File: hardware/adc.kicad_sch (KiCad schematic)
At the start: 21 parts, among them U5 NAU7802SGI, U7 NAU7802SGI

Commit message: Connect each ADC to a separate I2C bus
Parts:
- added R11, R12: 10kΩ, symbol Device:R_Small
- renumbered R11 to R13, R12 to R14
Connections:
- net +3.3V: now also R11.1, R12.1
- net SCLK renamed SCLK1
- net SCLK1: no longer U7.13 (SCLK)
- net SDIO renamed SDIO1
- net SDIO1: no longer U7.14 (SDIO)
- new net SCLK2: R12.2, U7.13 (SCLK)
- new net SDIO2: R11.2, U7.14 (SDIO)
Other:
- moved on the sheet: C17, C18, C19, C20, C21, R7, R8

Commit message: Assign footprints to symbols
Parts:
- C17, C18, C19, C20, C21, C22, C23, C24, C25, C26, C27, C28, C29: footprint (none) -> Capacitor_SMD:C_0603_1608Metric
- R10, R11, R12, R13, R14, R7, R8, R9: footprint (none) -> Resistor_SMD:R_0603_1608Metric
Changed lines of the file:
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@@
       (effects (font (size 1.27 1.27)) (justify left))
     )
-    (property "Footprint" "" (id 2) (at 187.96 80.01 0)
+    (property "Footprint" "Capacitor_SMD:C_0603_1608Metric" (id 2) (at 187.96 80.01 0)
       (effects (font (size 1.27 1.27)) hide)
     )
@@
       (effects (font (size 1.27 1.27)) (justify left))
     )
-    (property "Footprint" "" (id 2) (at 92.71 95.25 0)
+    (property "Footprint" "Capacitor_SMD:C_0603_1608Metric" (id 2) (at 92.71 95.25 0)
       (effects (font (size 1.27 1.27)) hide)
     )
@@
       (effects (font (size 1.27 1.27)) (justify left))
     )
-    (property "Footprint" "" (id 2) (at 170.18 82.55 0)
+    (property "Footprint" "Capacitor_SMD:C_0603_1608Metric" (id 2) (at 170.18 82.55 0)
       (effects (font (size 1.27 1.27)) hide)
     )
@@
     (property "Reference" "R13" (id 0) (at 173.99 106.68 90))
     (property "Value" "51Ω" (id 1) (at 182.88 106.68 90))
-    (property "Footprint" "" (id 2) (at 177.8 107.95 0)
+    (property "Footprint" "Resistor_SMD:R_0603_1608Metric" (id 2) (at 177.8 107.95 0)
       (effects (font (size 1.27 1.27)) hide)
     )
@@
       (effects (font (size 1.27 1.27)) (justify left))
     )
-    (property "Footprint" "" (id 2) (at 170.18 137.16 0)
+    (property "Footprint" "Capacitor_SMD:C_0603_1608Metric" (id 2) (at 170.18 137.16 0)
       (effects (font (size 1.27 1.27)) hide)
     )
@@
       (effects (font (size 1.27 1.27)) (justify left))
     )
-    (property "Footprint" "" (id 2) (at 133.35 107.95 0)
+    (property "Footprint" "Resistor_SMD:R_0603_1608Metric" (id 2) (at 133.35 107.95 0)
       (effects (font (size 1.27 1.27)) hide)
     )
@@
       (effects (font (size 1.27 1.27)) (justify left))
     )
-    (property "Footprint" "" (id 2) (at 187.96 111.76 0)
+    (property "Footprint" "Capacitor_SMD:C_0603_1608Metric" (id 2) (at 187.96 111.76 0)
       (effects (font (size 1.27 1.27)) hide)
     )
@@
       (effects (font (size 1.27 1.27)) (justify left))
     )
-    (property "Footprint" "" (id 2) (at 173.99 121.92 0)
+    (property "Footprint" "Capacitor_SMD:C_0603_1608Metric" (id 2) (at 173.99 121.92 0)
       (effects (font (size 1.27 1.27)) hide)
     )
@@
       (effects (font (size 1.27 1.27)) (justify left))
     )
-    (property "Footprint" "" (id 2) (at 66.04 95.25 0)
+    (property "Footprint" "Capacitor_SMD:C_0603_1608Metric" (id 2) (at 66.04 95.25 0)
       (effects (font (size 1.27 1.27)) hide)
     )
@@
       (effects (font (size 1.27 1.27)) (justify left))
     )
-    (property "Footprint" "" (id 2) (at 133.35 53.34 0)
+    (property "Footprint" "Resistor_SMD:R_0603_1608Metric" (id 2) (at 133.35 53.34 0)
       (effects (font (size 1.27 1.27)) hide)
     )
@@
     (property "Reference" "R10" (id 0) (at 173.99 59.69 90))
     (property "Value" "51Ω" (id 1) (at 182.88 59.69 90))
-    (property "Footprint" "" (id 2) (at 177.8 60.96 0)
+    (property "Footprint" "Resistor_SMD:R_0603_1608Metric" (id 2) (at 177.8 60.96 0)
       (effects (font (size 1.27 1.27)) hide)
     )
@@
     (property "Reference" "R14" (id 0) (at 173.99 114.3 90))
     (property "Value" "51Ω" (id 1) (at 182.88 114.3 90))
-    (property "Footprint" "" (id 2) (at 177.8 115.57 0)
+    (property "Footprint" "Resistor_SMD:R_0603_1608Metric" (id 2) (at 177.8 115.57 0)
       (effects (font (size 1.27 1.27)) hide)
     )
@@
       (effects (font (size 1.27 1.27)) (justify left))
     )
-    (property "Footprint" "" (id 2) (at 173.99 67.31 0)
+    (property "Footprint" "Capacitor_SMD:C_0603_1608Metric" (id 2) (at 173.99 67.31 0)
       (effects (font (size 1.27 1.27)) hide)
     )
@@
       (effects (font (size 1.27 1.27)) (justify left))
     )
-    (property "Footprint" "" (id 2) (at 187.96 134.62 0)
+    (property "Footprint" "Capacitor_SMD:C_0603_1608Metric" (id 2) (at 187.96 134.62 0)
       (effects (font (size 1.27 1.27)) hide)
     )
@@
       (effects (font (size 1.27 1.27)) (justify left))
     )
-    (property "Footprint" "" (id 2) (at 74.93 95.25 0)
+    (property "Footprint" "Capacitor_SMD:C_0603_1608Metric" (id 2) (at 74.93 95.25 0)
       (effects (font (size 1.27 1.27)) hide)
     )
@@
     (property "Reference" "R9" (id 0) (at 173.99 52.07 90))
     (property "Value" "51Ω" (id 1) (at 182.88 52.07 90))
-    (property "Footprint" "" (id 2) (at 177.8 53.34 0)
+    (property "Footprint" "Resistor_SMD:R_0603_1608Metric" (id 2) (at 177.8 53.34 0)
       (effects (font (size 1.27 1.27)) hide)
     )
@@
       (effects (font (size 1.27 1.27)) (justify left))
     )
-    (property "Footprint" "" (id 2) (at 187.96 57.15 0)
+    (property "Footprint" "Capacitor_SMD:C_0603_1608Metric" (id 2) (at 187.96 57.15 0)
       (effects (font (size 1.27 1.27)) hide)
     )
@@
       (effects (font (size 1.27 1.27)) (justify left))
     )
-    (property "Footprint" "" (id 2) (at 83.82 95.25 0)
+    (property "Footprint" "Capacitor_SMD:C_0603_1608Metric" (id 2) (at 83.82 95.25 0)
       (effects (font (size 1.27 1.27)) hide)
     )
@@
       (effects (font (size 1.27 1.27)) (justify left))
     )
-    (property "Footprint" "" (id 2) (at 127 53.34 0)
+    (property "Footprint" "Resistor_SMD:R_0603_1608Metric" (id 2) (at 127 53.34 0)
       (effects (font (size 1.27 1.27)) hide)
     )
@@
       (effects (font (size 1.27 1.27)) (justify left))
     )
-    (property "Footprint" "" (id 2) (at 127 107.95 0)
+    (property "Footprint" "Resistor_SMD:R_0603_1608Metric" (id 2) (at 127 107.95 0)
       (effects (font (size 1.27 1.27)) hide)
     )
@@
       (effects (font (size 1.27 1.27)) (justify left))
     )
-    (property "Footprint" "" (id 2) (at 57.15 95.25 0)
-      (effects (font (size 1.27 1.27)) hide)
-    )
+    (property "Footprint" "Capacitor_SMD:C_0603_1608Metric" (id 2) (at 57.15 95.25 0)
+      (effects (font (size 1.27 1.27)) hide)
+    )

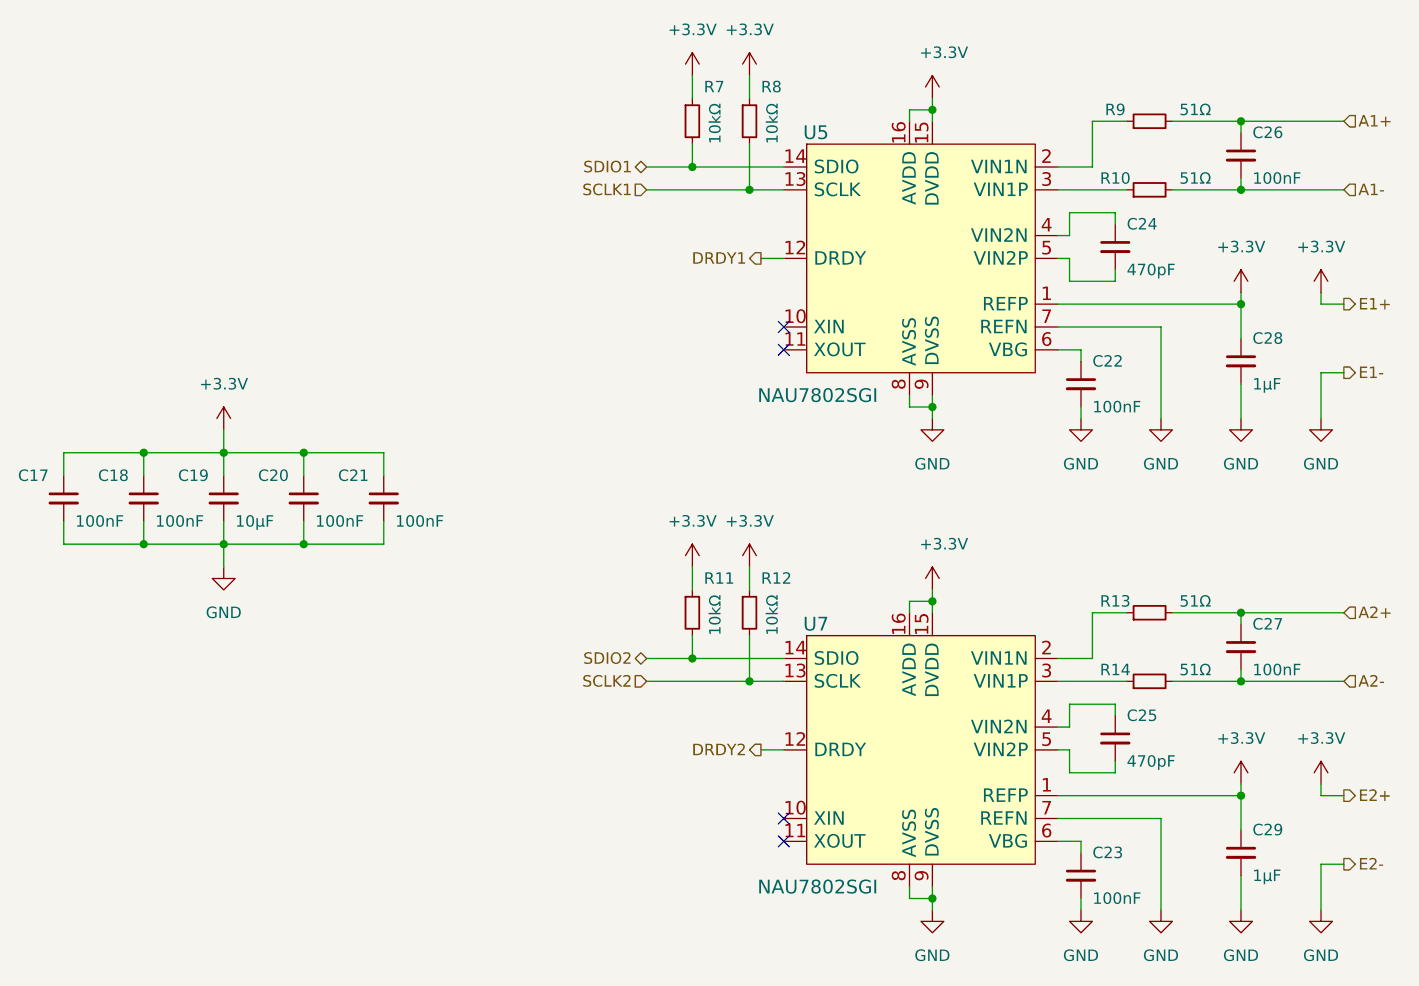
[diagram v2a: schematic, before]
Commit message: Use more efficient buck converter
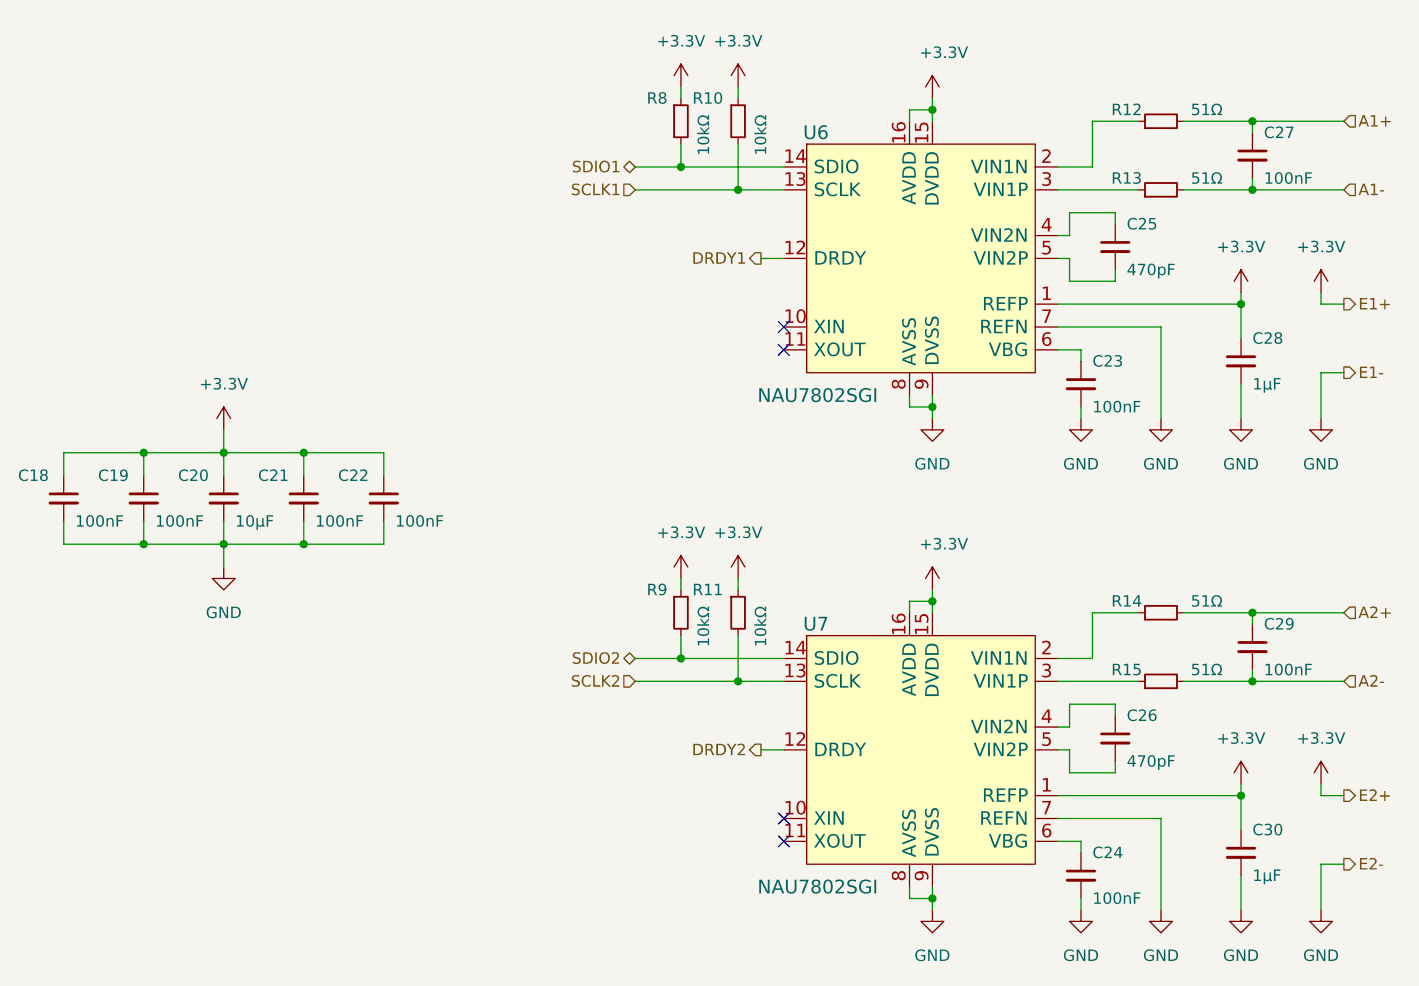
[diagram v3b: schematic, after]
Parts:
- renumbered C17 to C18, C18 to C19, C19 to C20, C20 to C21, C21 to C22, C22 to C23, C23 to C24, C24 to C25, C25 to C26, C26 to C27, C27 to C29, C29 to C30, R8 to R10, R12 to R11, R9 to R12, R10 to R13, R13 to R14, R14 to R15, R7 to R8, R11 to R9, U5 to U6
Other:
- moved on the sheet: C27, C29, R10, R11, R12, R13, R14, R15, R8, R9

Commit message: Apply PUTM branding
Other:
- company: PUT Motorsport -> Author: I. Kajdan
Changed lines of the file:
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@@
   (title_block
     (title "ADC")
-    (date "2022-12-10")
+    (date "2022-12-11")
     (rev "${REVISION}")
-    (company "PUT Motorsport")
-    (comment 3 "Reviewer:")
-    (comment 4 "Author: I. Kajdan")
+    (company "Author: I. Kajdan")
   )
   (junction (at 189.23 60.96) (diameter 0) (color 0 0 0 0)

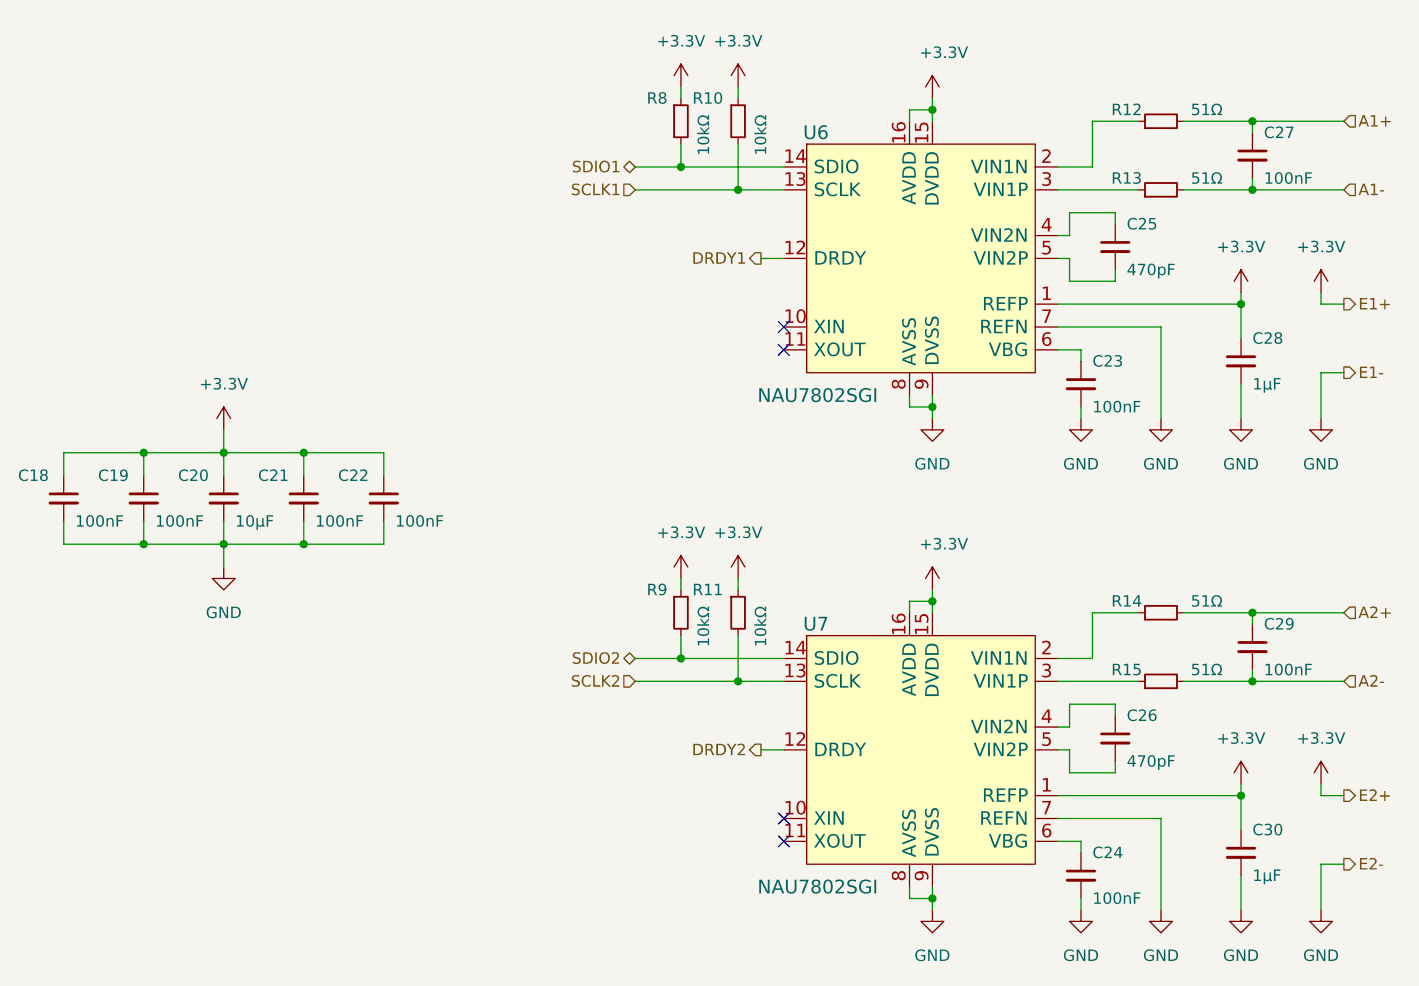
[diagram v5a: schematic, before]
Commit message: Miscellaneous changes
- Use THT connectors
- Adjust ADC circuit according to the datasheet
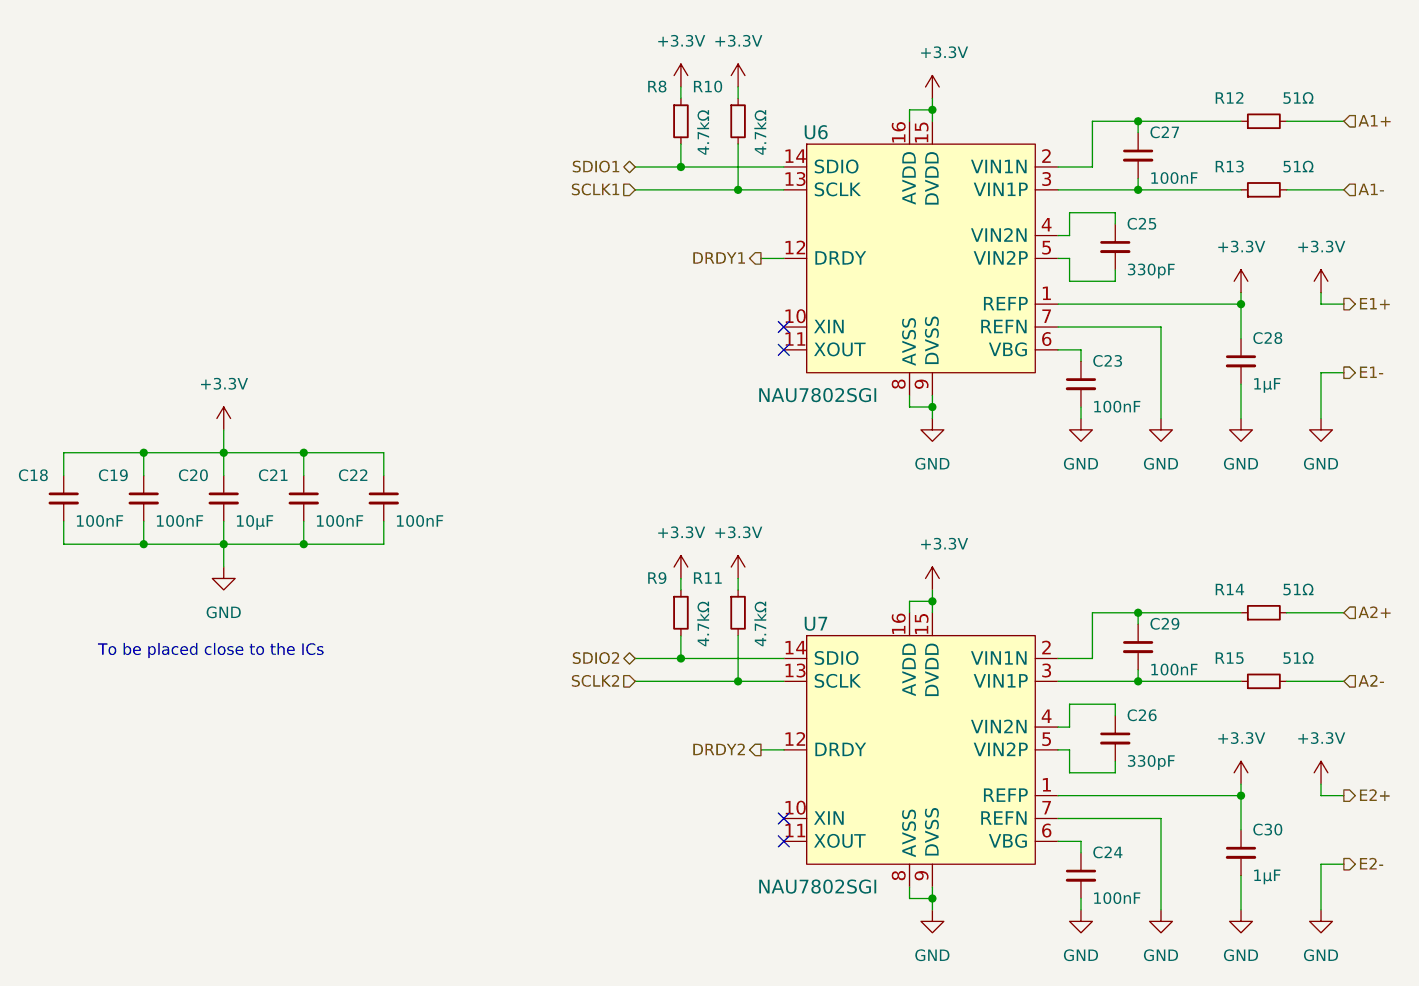
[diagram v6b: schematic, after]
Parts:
- C25, C26: value 470pF -> 330pF
- R10, R11, R8, R9: value 10kΩ -> 4.7kΩ
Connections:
- net A1+: no longer C27.1
- net A1-: no longer C27.2
- net A2+: no longer C29.1
- net A2-: no longer C29.2
- net at R14.1, U7.2 (VIN1N): now also C29.1
- net at R15.1, U7.3 (VIN1P): now also C29.2
- net at R12.1, U6.2 (VIN1N): now also C27.1
- net at R13.1, U6.3 (VIN1P): now also C27.2
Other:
- note added: "To be placed close to the ICs"
- moved on the sheet: C27, C29, R12, R13, R14, R15
